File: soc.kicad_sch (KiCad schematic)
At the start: 89 parts, among them U1 MPFS250T-FCVG484

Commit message: [#54016] Change 100nF to 0201 package
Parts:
- C12, C14, C15, C16, C17, C18, C19, C2, C3, C34, C37, C39, C4, C40, C41, C43, C45, C46, C6, C61, C62, C63, C7, C8: value C_100n_0402 -> C_100n_0201_25V; footprint antmicro-footprints:C_0402_1005Metric -> antmicro-footprints:C_0201; symbol antmicroCapacitors0402:C_100n_0402 -> antmicroCapacitorsmisc:C_100n_0201_25V; MPN GRM155R61H104KE14D -> C0603X5R1E104K030BB; Manufacturer Murata -> TDK; Voltage 50V -> 25V

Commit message: [#54016] Reconnect decoupling capacitors in more compact way
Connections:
- net +1V8: no longer C55.2
- net XCVR_VREF: now reaches R16.2, U1.H18 (XCVR_VREF), U1.H19 (XCVR_VREF)
- net XCVR_VREF: now also C4.2, C8.2
- net at C20.2: now also C12.2, C16.2
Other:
- moved on the sheet: C1, C10, C11, C12, C13, C14, C15, C16, C17, C18, C19, C2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

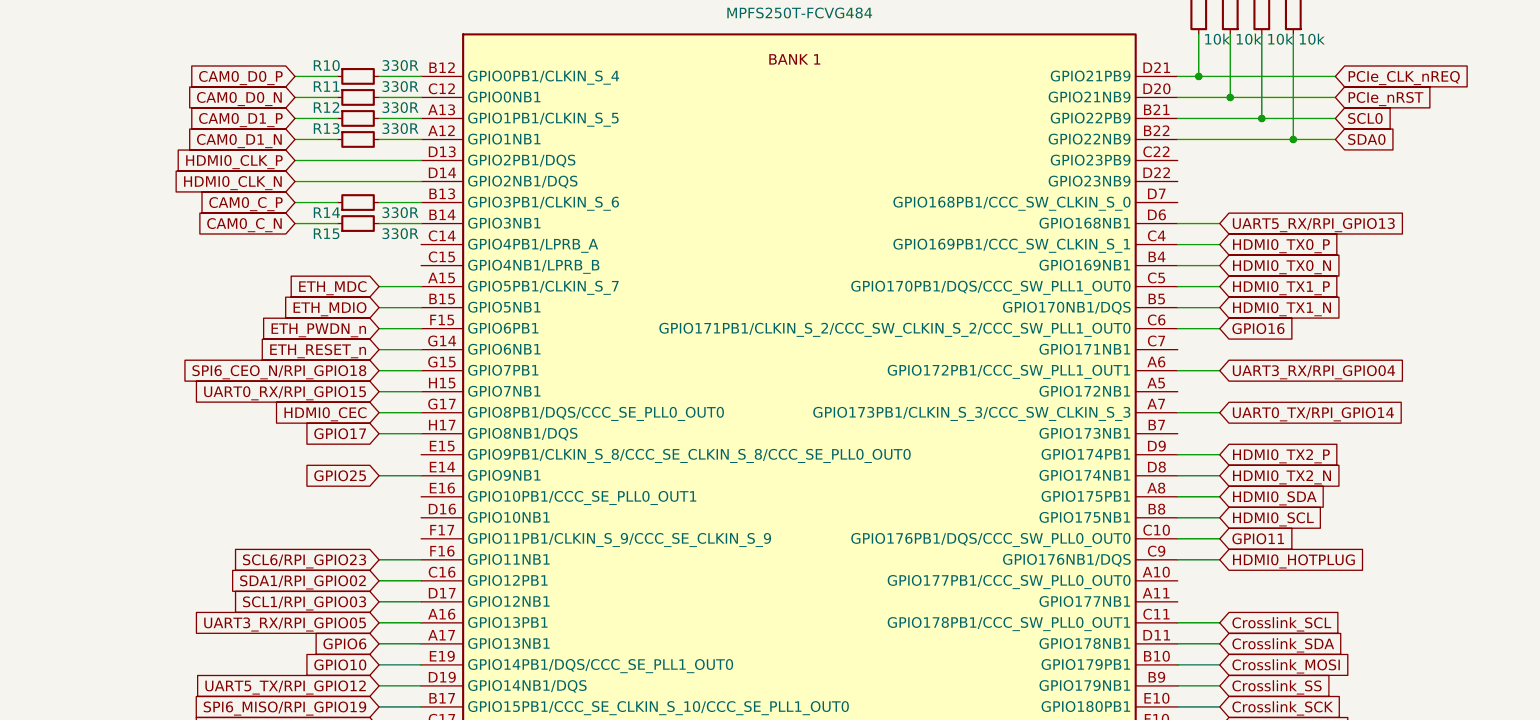
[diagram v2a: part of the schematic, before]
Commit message: [#53847] Add SN75DP159RSBT to HDMI schematic
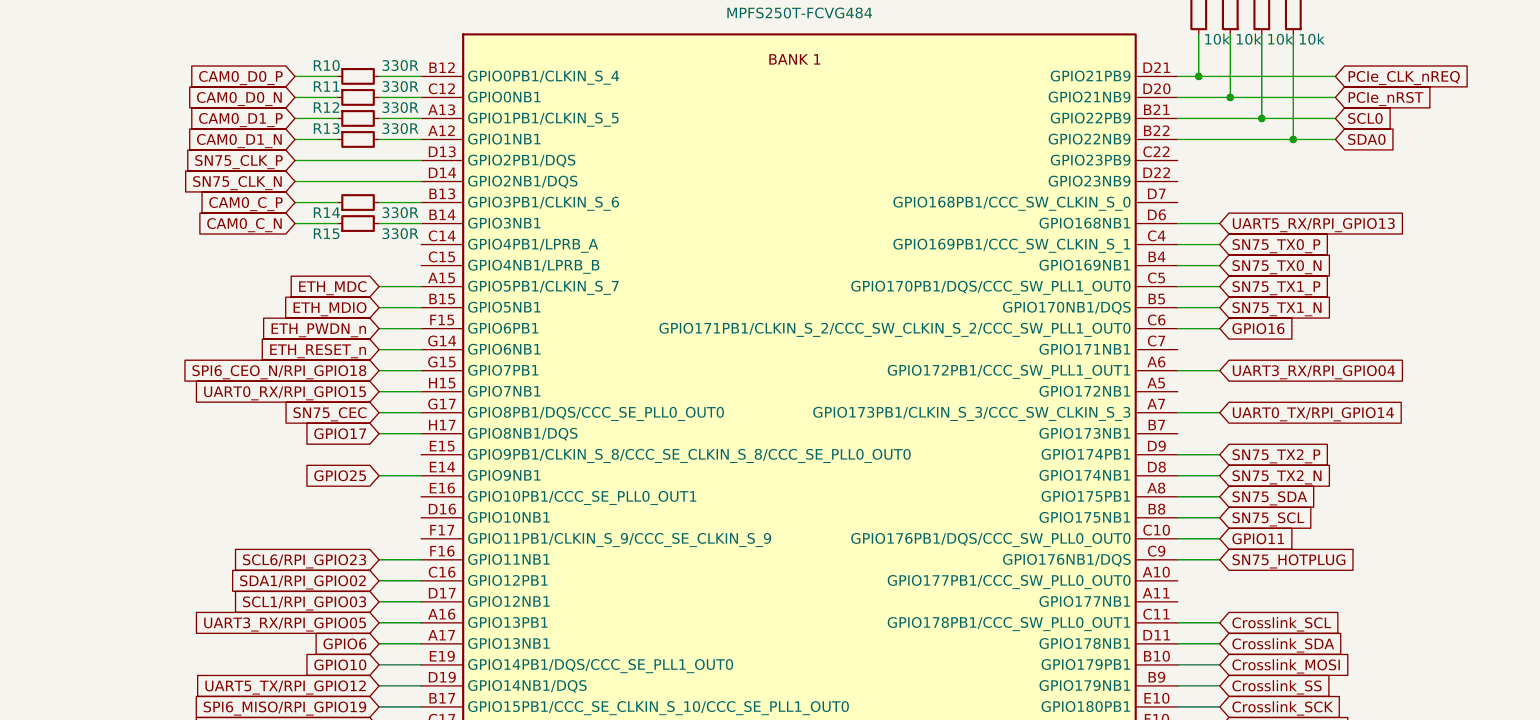
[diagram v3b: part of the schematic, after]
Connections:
- net HDMI0_CEC renamed SN75_CEC
- net HDMI0_CLK_N renamed SN75_CLK_N
- net HDMI0_CLK_P renamed SN75_CLK_P
- net HDMI0_HOTPLUG renamed SN75_HOTPLUG
- net HDMI0_SCL renamed SN75_SCL
- net HDMI0_SDA renamed SN75_SDA
- net HDMI0_TX0_N renamed SN75_TX0_N
- net HDMI0_TX0_P renamed SN75_TX0_P
- net HDMI0_TX1_N renamed SN75_TX1_N
- net HDMI0_TX1_P renamed SN75_TX1_P
- net HDMI0_TX2_N renamed SN75_TX2_N
- net HDMI0_TX2_P renamed SN75_TX2_P
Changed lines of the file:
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@@
     )
   )
-  (global_label "HDMI0_TX0_P" (shape input) (at 350.52 67.31 0) (fields_autoplaced)
-    (effects (font (size 1.27 1.27)) (justify left))
-    (property "Intersheetrefs" "${INTERSHEET_REFS}" (at 365.3912 67.2306 0)
+  (global_label "SN75_TX0_P" (shape input) (at 350.52 67.31 0) (fields_autoplaced)
+    (effects (font (size 1.27 1.27)) (justify left))
+    (property "Intersheetrefs" "${INTERSHEET_REFS}" (at 365.056 67.31 0)
       (effects (font (size 1.27 1.27)) (justify left) hide)
     )
@@
     )
   )
-  (global_label "HDMI0_TX1_P" (shape input) (at 350.52 72.39 0) (fields_autoplaced)
-    (effects (font (size 1.27 1.27)) (justify left))
-    (property "Intersheetrefs" "${INTERSHEET_REFS}" (at 365.3912 72.3106 0)
+  (global_label "SN75_TX1_P" (shape input) (at 350.52 72.39 0) (fields_autoplaced)
+    (effects (font (size 1.27 1.27)) (justify left))
+    (property "Intersheetrefs" "${INTERSHEET_REFS}" (at 365.056 72.39 0)
       (effects (font (size 1.27 1.27)) (justify left) hide)
     )
@@
     )
   )
-  (global_label "HDMI0_TX2_P" (shape input) (at 350.52 92.71 0) (fields_autoplaced)
-    (effects (font (size 1.27 1.27)) (justify left))
-    (property "Intersheetrefs" "${INTERSHEET_REFS}" (at 365.3912 92.6306 0)
+  (global_label "SN75_TX2_P" (shape input) (at 350.52 92.71 0) (fields_autoplaced)
+    (effects (font (size 1.27 1.27)) (justify left))
+    (property "Intersheetrefs" "${INTERSHEET_REFS}" (at 365.056 92.71 0)
       (effects (font (size 1.27 1.27)) (justify left) hide)
     )
@@
     )
   )
-  (global_label "HDMI0_CLK_P" (shape input) (at 238.76 57.15 180) (fields_autoplaced)
-    (effects (font (size 1.27 1.27)) (justify right))
-    (property "Intersheetrefs" "${INTERSHEET_REFS}" (at 223.7074 57.0706 0)
+  (global_label "SN75_CLK_P" (shape input) (at 238.76 57.15 180) (fields_autoplaced)
+    (effects (font (size 1.27 1.27)) (justify right))
+    (property "Intersheetrefs" "${INTERSHEET_REFS}" (at 224.0425 57.15 0)
       (effects (font (size 1.27 1.27)) (justify right) hide)
     )
@@
     )
   )
-  (global_label "HDMI0_SCL" (shape input) (at 350.52 100.33 0) (fields_autoplaced)
-    (effects (font (size 1.27 1.27)) (justify left))
-    (property "Intersheetrefs" "${INTERSHEET_REFS}" (at 363.2745 100.2506 0)
+  (global_label "SN75_SCL" (shape input) (at 350.52 100.33 0) (fields_autoplaced)
+    (effects (font (size 1.27 1.27)) (justify left))
+    (property "Intersheetrefs" "${INTERSHEET_REFS}" (at 362.9394 100.33 0)
       (effects (font (size 1.27 1.27)) (justify left) hide)
     )
@@
     )
   )
-  (global_label "HDMI0_CLK_N" (shape input) (at 238.76 59.69 180) (fields_autoplaced)
-    (effects (font (size 1.27 1.27)) (justify right))
-    (property "Intersheetrefs" "${INTERSHEET_REFS}" (at 223.6469 59.6106 0)
-      (effects (font (size 1.27 1.27)) (justify right) hide)
-    )
-  )
-  (global_label "HDMI0_TX0_N" (shape input) (at 350.52 69.85 0) (fields_autoplaced)
-    (effects (font (size 1.27 1.27)) (justify left))
-    (property "Intersheetrefs" "${INTERSHEET_REFS}" (at 365.4517 69.7706 0)
+  (global_label "SN75_CLK_N" (shape input) (at 238.76 59.69 180) (fields_autoplaced)
+    (effects (font (size 1.27 1.27)) (justify right))
+    (property "Intersheetrefs" "${INTERSHEET_REFS}" (at 223.982 59.69 0)
+      (effects (font (size 1.27 1.27)) (justify right) hide)
+    )
+  )
+  (global_label "SN75_TX0_N" (shape input) (at 350.52 69.85 0) (fields_autoplaced)
+    (effects (font (size 1.27 1.27)) (justify left))
+    (property "Intersheetrefs" "${INTERSHEET_REFS}" (at 365.1165 69.85 0)
       (effects (font (size 1.27 1.27)) (justify left) hide)
     )
@@
     )
   )
-  (global_label "HDMI0_CEC" (shape input) (at 248.92 87.63 180) (fields_autoplaced)
-    (effects (font (size 1.27 1.27)) (justify right))
-    (property "Intersheetrefs" "${INTERSHEET_REFS}" (at 235.984 87.5506 0)
+  (global_label "SN75_CEC" (shape input) (at 248.92 87.63 180) (fields_autoplaced)
+    (effects (font (size 1.27 1.27)) (justify right))
+    (property "Intersheetrefs" "${INTERSHEET_REFS}" (at 236.3192 87.63 0)
       (effects (font (size 1.27 1.27)) (justify right) hide)
     )
@@
     )
   )
-  (global_label "HDMI0_TX1_N" (shape input) (at 350.52 74.93 0) (fields_autoplaced)
-    (effects (font (size 1.27 1.27)) (justify left))
-    (property "Intersheetrefs" "${INTERSHEET_REFS}" (at 365.4517 74.8506 0)
+  (global_label "SN75_TX1_N" (shape input) (at 350.52 74.93 0) (fields_autoplaced)
+    (effects (font (size 1.27 1.27)) (justify left))
+    (property "Intersheetrefs" "${INTERSHEET_REFS}" (at 365.1165 74.93 0)
       (effects (font (size 1.27 1.27)) (justify left) hide)
     )
@@
     )
   )
-  (global_label "HDMI0_TX2_N" (shape input) (at 350.52 95.25 0) (fields_autoplaced)
-    (effects (font (size 1.27 1.27)) (justify left))
-    (property "Intersheetrefs" "${INTERSHEET_REFS}" (at 365.4517 95.1706 0)
+  (global_label "SN75_TX2_N" (shape input) (at 350.52 95.25 0) (fields_autoplaced)
+    (effects (font (size 1.27 1.27)) (justify left))
+    (property "Intersheetrefs" "${INTERSHEET_REFS}" (at 365.1165 95.25 0)
       (effects (font (size 1.27 1.27)) (justify left) hide)
     )
@@
     )
   )
-  (global_label "HDMI0_HOTPLUG" (shape input) (at 350.52 105.41 0) (fields_autoplaced)
-    (effects (font (size 1.27 1.27)) (justify left))
-    (property "Intersheetrefs" "${INTERSHEET_REFS}" (at 368.2941 105.3306 0)
+  (global_label "SN75_HOTPLUG" (shape input) (at 350.52 105.41 0) (fields_autoplaced)
+    (effects (font (size 1.27 1.27)) (justify left))
+    (property "Intersheetrefs" "${INTERSHEET_REFS}" (at 367.959 105.41 0)
       (effects (font (size 1.27 1.27)) (justify left) hide)
     )
@@
     )
   )
-  (global_label "HDMI0_SDA" (shape input) (at 350.52 97.79 0) (fields_autoplaced)
-    (effects (font (size 1.27 1.27)) (justify left))
-    (property "Intersheetrefs" "${INTERSHEET_REFS}" (at 363.335 97.7106 0)
-      (effects (font (size 1.27 1.27)) (justify left) hide)
-    )
+  (global_label "SN75_SDA" (shape input) (at 350.52 97.79 0) (fields_autoplaced)
+    (effects (font (size 1.27 1.27)) (justify left))
+    (property "Intersheetrefs" "${INTERSHEET_REFS}" (at 362.9999 97.79 0)
+      (effects (font (size 1.27 1.27)) (justify left) hide)
+    )

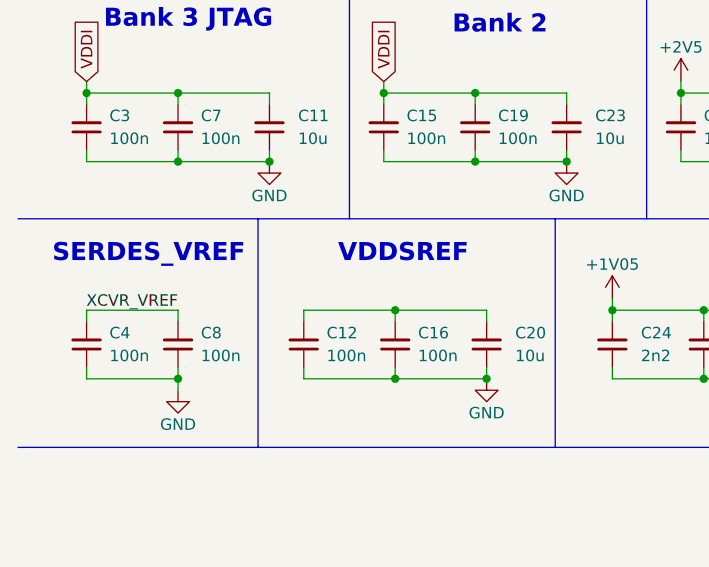
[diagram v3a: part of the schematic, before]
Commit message: [#54016] Connect VDDSREF decoupling capacitors
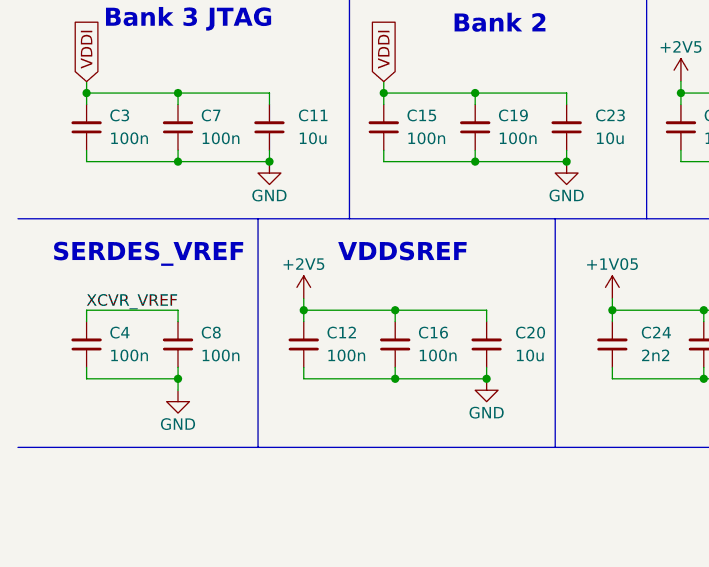
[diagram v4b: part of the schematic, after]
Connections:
- net +2V5: now also C12.2, C16.2, C20.2
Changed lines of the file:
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@@
   (junction (at 73.66 196.85) (diameter 0) (color 0 0 0 0)
   )
+  (junction (at 44.45 240.03) (diameter 0) (color 0 0 0 0)
+  )
   (junction (at 129.54 189.23) (diameter 0) (color 0 0 0 0)
   )
@@
     (stroke (width 0) (type default))
   )
+  (wire (pts (xy 44.45 238.76) (xy 44.45 240.03))
+    (stroke (width 0) (type default))
+  )
   (wire (pts (xy 119.38 189.23) (xy 119.38 190.5))
     (stroke (width 0) (type default))
@@
         )
       )
+    )
+  )
+  (symbol (lib_id "antmicropower:+2V5") (at 44.45 238.76 0) (unit 1)
+    (in_bom yes) (on_board yes) (dnp no)
+    (property "Reference" "#PWR024" (at 44.45 242.57 0)
+      (effects (font (size 1.27 1.27)) hide)
+    )
+    (property "Value" "+2V5" (at 44.45 234.95 0)
+      (effects (font (size 1.27 1.27)))
+    )
+    (property "Footprint" "" (at 44.45 238.76 0)
+      (effects (font (size 1.27 1.27)) hide)
+    )
+    (property "Datasheet" "" (at 44.45 238.76 0)
+      (effects (font (size 1.27 1.27)) hide)
+    )
+    (pin "1")
+    (instances
+      (project "polarfire-som"
+        (path "/db4a0d3e-2eb3-499e-977d-6eb378cfd3ed/99f116ae-bc8e-42a5-8f88-aecc401b3bcc"
+          (reference "#PWR024") (unit 1)
+        )
+      )

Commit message: [#53847] Add HDMI
[#53847] Add HDMI driver power decoupling
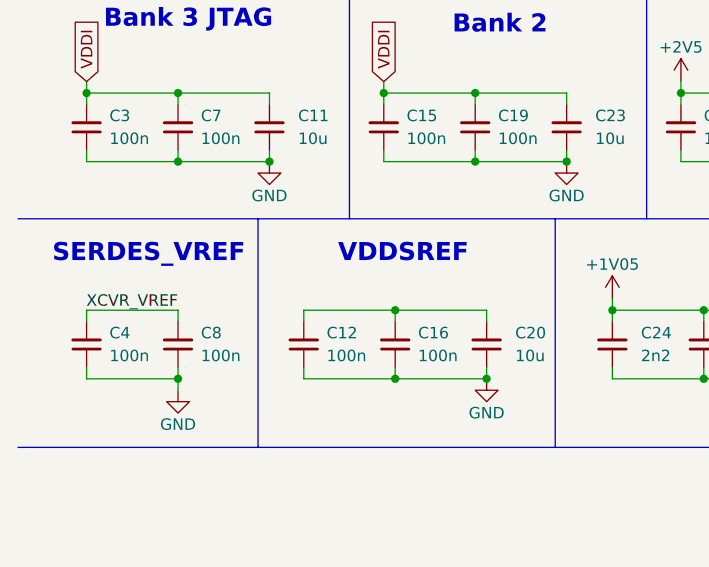
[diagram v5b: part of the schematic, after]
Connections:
- net +2V5: no longer C12.2, C16.2, C20.2
- new net: C12.2, C16.2, C20.2
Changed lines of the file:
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@@
   (junction (at 73.66 196.85) (diameter 0) (color 0 0 0 0)
   )
-  (junction (at 44.45 240.03) (diameter 0) (color 0 0 0 0)
-  )
   (junction (at 129.54 189.23) (diameter 0) (color 0 0 0 0)
   )
@@
     (stroke (width 0) (type default))
   )
-  (wire (pts (xy 44.45 238.76) (xy 44.45 240.03))
-    (stroke (width 0) (type default))
-  )
   (wire (pts (xy 119.38 189.23) (xy 119.38 190.5))
     (stroke (width 0) (type default))
@@
         )
       )
-    )
-  )
-  (symbol (lib_id "antmicropower:+2V5") (at 44.45 238.76 0) (unit 1)
-    (in_bom yes) (on_board yes) (dnp no)
-    (property "Reference" "#PWR024" (at 44.45 242.57 0)
-      (effects (font (size 1.27 1.27)) hide)
-    )
-    (property "Value" "+2V5" (at 44.45 234.95 0)
-      (effects (font (size 1.27 1.27)))
-    )
-    (property "Footprint" "" (at 44.45 238.76 0)
-      (effects (font (size 1.27 1.27)) hide)
-    )
-    (property "Datasheet" "" (at 44.45 238.76 0)
-      (effects (font (size 1.27 1.27)) hide)
-    )
-    (pin "1")
-    (instances
-      (project "polarfire-som"
-        (path "/db4a0d3e-2eb3-499e-977d-6eb378cfd3ed/99f116ae-bc8e-42a5-8f88-aecc401b3bcc"
-          (reference "#PWR024") (unit 1)
-        )
-      )

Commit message: [#54899] Simplify power sequencing, add missing connections
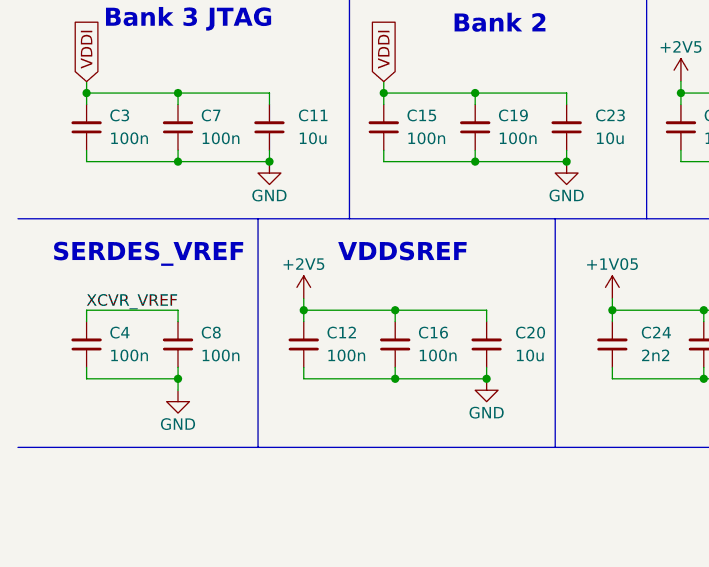
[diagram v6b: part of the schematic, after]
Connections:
- net +2V5: now also C12.2, C16.2, C20.2
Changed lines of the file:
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@@
   (junction (at 119.38 247.65) (diameter 0) (color 0 0 0 0)
   )
+  (junction (at 44.45 240.03) (diameter 0) (color 0 0 0 0)
+  )
   (junction (at 96.52 223.52) (diameter 0) (color 0 0 0 0)
   )
@@
     (stroke (width 0) (type default))
   )
+  (wire (pts (xy 44.45 238.76) (xy 44.45 240.03))
+    (stroke (width 0) (type default))
+  )
   (wire (pts (xy 45.72 93.98) (xy 50.8 93.98))
     (stroke (width 0) (type default))
@@
         )
       )
+    )
+  )
+  (symbol (lib_id "antmicropower:+2V5") (at 44.45 238.76 0) (unit 1)
+    (in_bom yes) (on_board yes) (dnp no)
+    (property "Reference" "#PWR055" (at 44.45 242.57 0)
+      (effects (font (size 1.27 1.27)) hide)
+    )
+    (property "Value" "+2V5" (at 44.45 234.95 0)
+      (effects (font (size 1.27 1.27)))
+    )
+    (property "Footprint" "" (at 44.45 238.76 0)
+      (effects (font (size 1.27 1.27)) hide)
+    )
+    (property "Datasheet" "" (at 44.45 238.76 0)
+      (effects (font (size 1.27 1.27)) hide)
+    )
+    (pin "1")
+    (instances
+      (project "polarfire-som"
+        (path "/db4a0d3e-2eb3-499e-977d-6eb378cfd3ed/99f116ae-bc8e-42a5-8f88-aecc401b3bcc"
+          (reference "#PWR055") (unit 1)
+        )
+      )

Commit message: [#54899] Re-annotate components
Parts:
- renumbered C26 to C25, C27 to C26, C28 to C27, C25 to C28, C30 to C29, C31 to C30, C32 to C31, C29 to C32, C34 to C33, C35 to C34, C36 to C35, C33 to C36, C39 to C37, C40 to C39, C37 to C40, C43 to C41, C44 to C43, C41 to C44, C47 to C45, C48 to C47, C45 to C48, C50 to C49, C49 to C50, C55 to C54, C54 to C55, R12 to R10, R13 to R11, R14 to R12, R15 to R13, R16 to R14, R75 to R15, R76 to R16, R77 to R17, R78 to R18, R7 to R19, R1 to R2, R8 to R20, R9 to R21, R2 to R3, R3 to R4, R4 to R5, R5 to R6, R6 to R7, R10 to R8, R11 to R9
